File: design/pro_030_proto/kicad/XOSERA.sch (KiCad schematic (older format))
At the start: 38 parts, among them IC16 74LS74, IC17 74HCT245, IC18 74HCT245, IC19 74HCT245, J10 Upduino_LHS, J11 Upduino_RHS, J12 Conn_01x06_Male, J13 PMOD_TOP, J14 PMOD_BOTTOM, J15 Conn_02x04_Counter_Clockwise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

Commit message: More tidy up
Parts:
- R34, R35, R36, R37, R38, R39, R40, R41: value R -> 100R
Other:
- note added: "All 100R"
- note removed: "All 470R"
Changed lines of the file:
@@
 P 5950 4600
 F 0 "R34" V 5950 4600 50  0000 C CNN
-F 1 "R" V 5834 4600 50  0001 C CNN
+F 1 "100R" V 5834 4600 50  0001 C CNN
 F 2 "rosco_m68k:R-0207_10" V 5880 4600 50  0001 C CNN
 F 3 "~" H 5950 4600 50  0001 C CNN
@@
 P 5950 4700
 F 0 "R35" V 5950 4700 50  0000 C CNN
-F 1 "R" V 5834 4700 50  0001 C CNN
+F 1 "100R" V 5834 4700 50  0001 C CNN
 F 2 "rosco_m68k:R-0207_10" V 5880 4700 50  0001 C CNN
 F 3 "~" H 5950 4700 50  0001 C CNN
@@
 P 5950 4800
 F 0 "R36" V 5950 4800 50  0000 C CNN
-F 1 "R" V 5834 4800 50  0001 C CNN
+F 1 "100R" V 5834 4800 50  0001 C CNN
 F 2 "rosco_m68k:R-0207_10" V 5880 4800 50  0001 C CNN
 F 3 "~" H 5950 4800 50  0001 C CNN
@@
 P 5950 4900
 F 0 "R37" V 5950 4900 50  0000 C CNN
-F 1 "R" V 5834 4900 50  0001 C CNN
+F 1 "100R" V 5834 4900 50  0001 C CNN
 F 2 "rosco_m68k:R-0207_10" V 5880 4900 50  0001 C CNN
 F 3 "~" H 5950 4900 50  0001 C CNN
@@
 P 5950 5000
 F 0 "R38" V 5950 5000 50  0000 C CNN
-F 1 "R" V 5834 5000 50  0001 C CNN
+F 1 "100R" V 5834 5000 50  0001 C CNN
 F 2 "rosco_m68k:R-0207_10" V 5880 5000 50  0001 C CNN
 F 3 "~" H 5950 5000 50  0001 C CNN
@@
 P 5950 5100
 F 0 "R39" V 5950 5100 50  0000 C CNN
-F 1 "R" V 5834 5100 50  0001 C CNN
+F 1 "100R" V 5834 5100 50  0001 C CNN
 F 2 "rosco_m68k:R-0207_10" V 5880 5100 50  0001 C CNN
 F 3 "~" H 5950 5100 50  0001 C CNN
@@
 P 5950 5300
 F 0 "R41" V 5950 5300 50  0000 C CNN
-F 1 "R" V 5834 5300 50  0001 C CNN
+F 1 "100R" V 5834 5300 50  0001 C CNN
 F 2 "rosco_m68k:R-0207_10" V 5880 5300 50  0001 C CNN
 F 3 "~" H 5950 5300 50  0001 C CNN
@@
 P 5950 5200
 F 0 "R40" V 5950 5200 50  0000 C CNN
-F 1 "R" V 5834 5200 50  0001 C CNN
+F 1 "100R" V 5834 5200 50  0001 C CNN
 F 2 "rosco_m68k:R-0207_10" V 5880 5200 50  0001 C CNN
 F 3 "~" H 5950 5200 50  0001 C CNN
@@
 $EndComp
 Text Notes 5800 5450 0    50   ~ 0
-All 470R
+All 100R
 Wire Wire Line
 	5800 4600 5700 4600

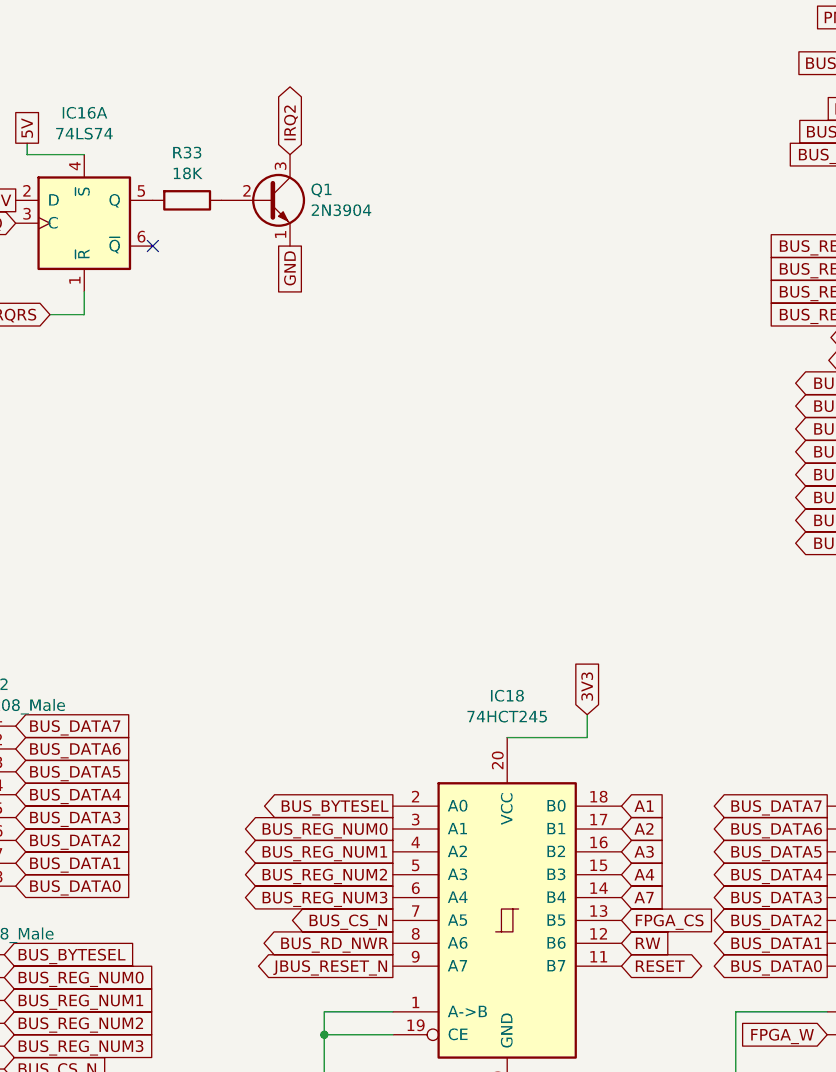
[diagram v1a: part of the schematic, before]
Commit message: Fix incorrect address line hookup for Xosera
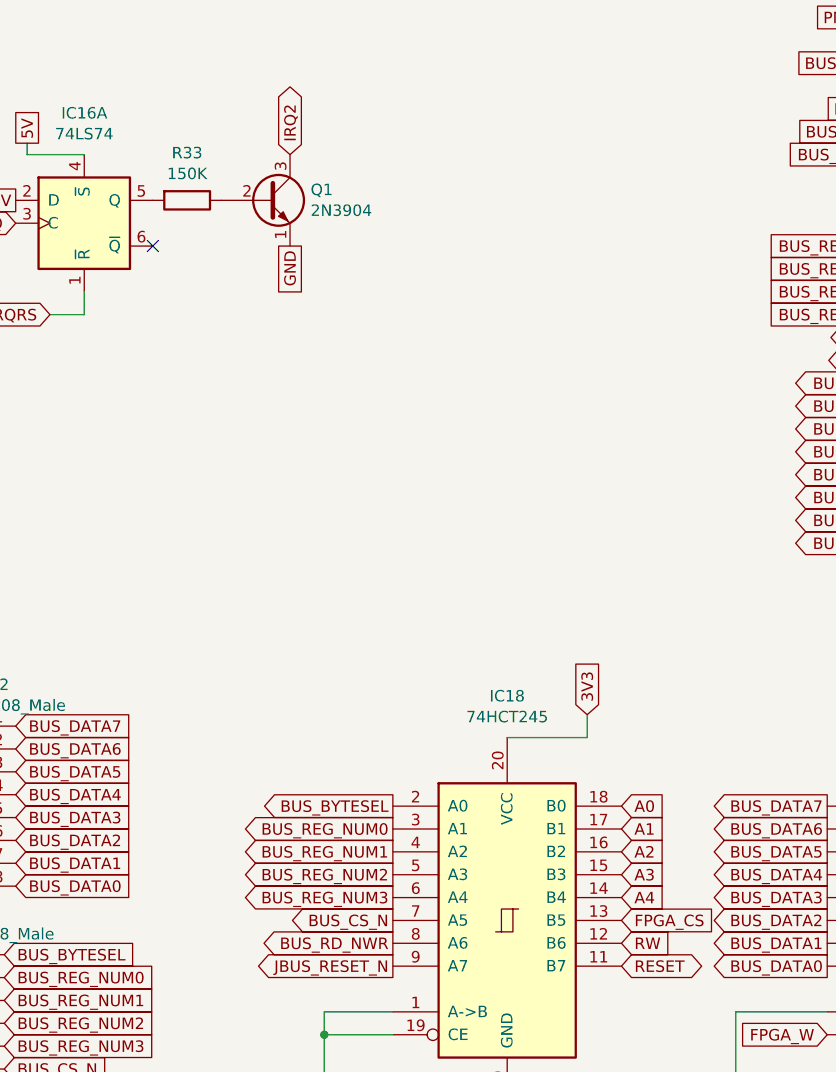
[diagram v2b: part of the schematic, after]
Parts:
- R33: value 18K -> 150K
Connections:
- net A7 is gone; now on net A4: IC18.14 (B4)
- net A1: now also IC18.17 (B1); no longer IC18.18 (B0)
- net A2: now also IC18.16 (B2); no longer IC18.17 (B1)
- net A3: now also IC18.15 (B3); no longer IC18.16 (B2)
- net A4: no longer IC18.15 (B3)
- new net A0: IC18.18 (B0)
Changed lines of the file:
@@
 FPGA_R
 Text GLabel 3800 4600 2    50   Input ~ 0
+A0
+Text GLabel 3800 4700 2    50   Input ~ 0
 A1
-Text GLabel 3800 4700 2    50   Input ~ 0
+Text GLabel 3800 4800 2    50   Input ~ 0
 A2
-Text GLabel 3800 4800 2    50   Input ~ 0
+Text GLabel 3800 4900 2    50   Input ~ 0
 A3
-Text GLabel 3800 4900 2    50   Input ~ 0
+Text GLabel 3800 5000 2    50   Input ~ 0
 A4
-Text GLabel 3800 5000 2    50   Input ~ 0
-A7
 Text GLabel 2800 4600 0    50   Output ~ 0
 BUS_BYTESEL
@@
 P 1900 1950
 F 0 "R33" V 1693 1950 50  0000 C CNN
-F 1 "18K" V 1784 1950 50  0000 C CNN
+F 1 "150K" V 1784 1950 50  0000 C CNN
 F 2 "rosco_m68k:R-0207_10" V 1830 1950 50  0001 C CNN
 F 3 "~" H 1900 1950 50  0001 C CNN

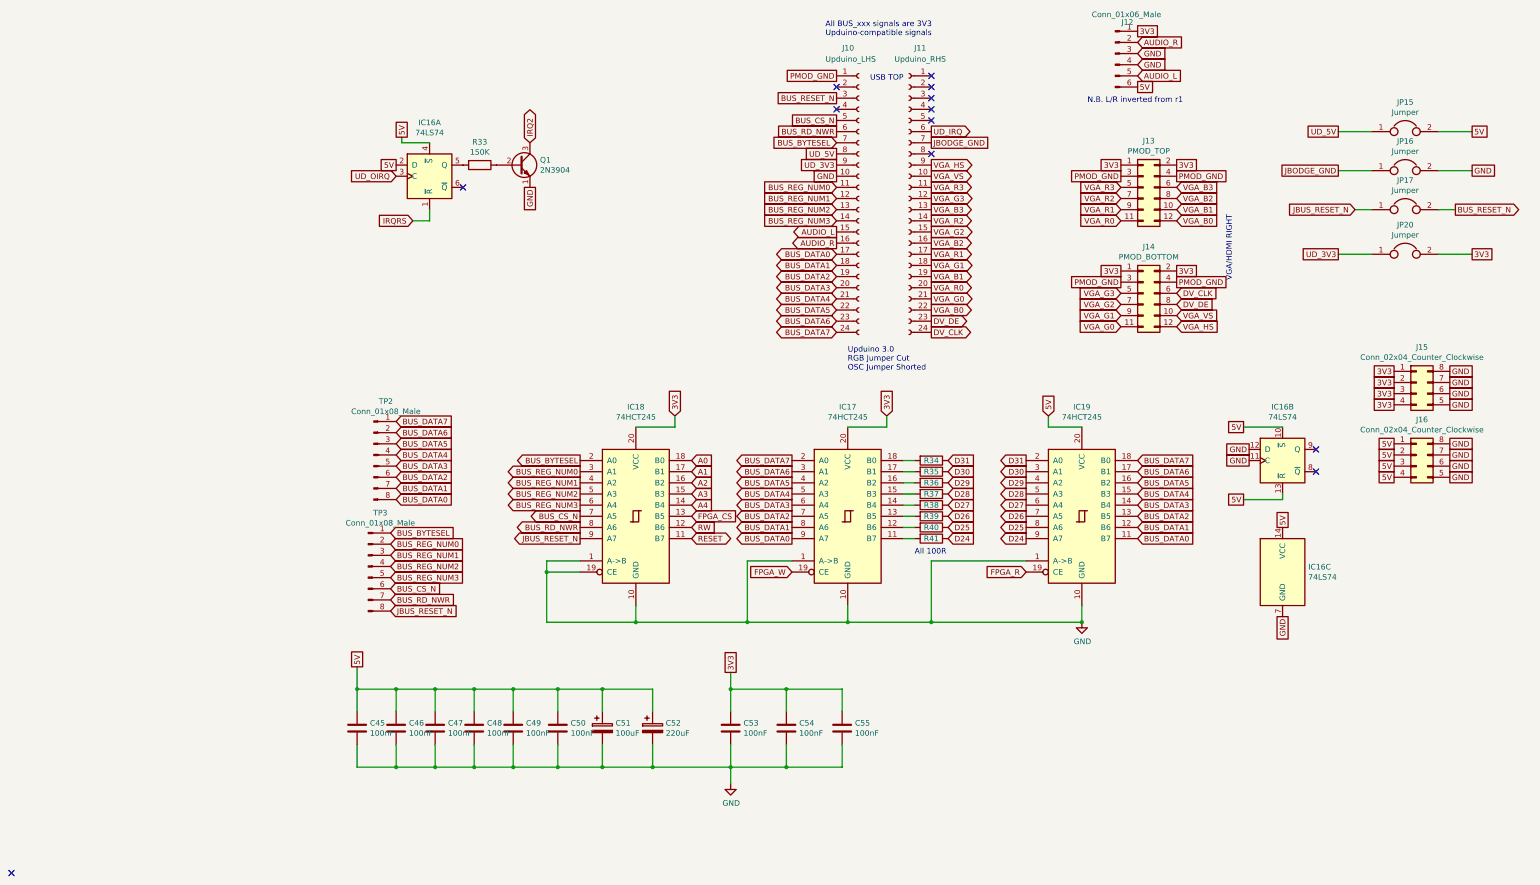
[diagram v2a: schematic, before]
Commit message: Add new Xosera DTACK stretch GAL
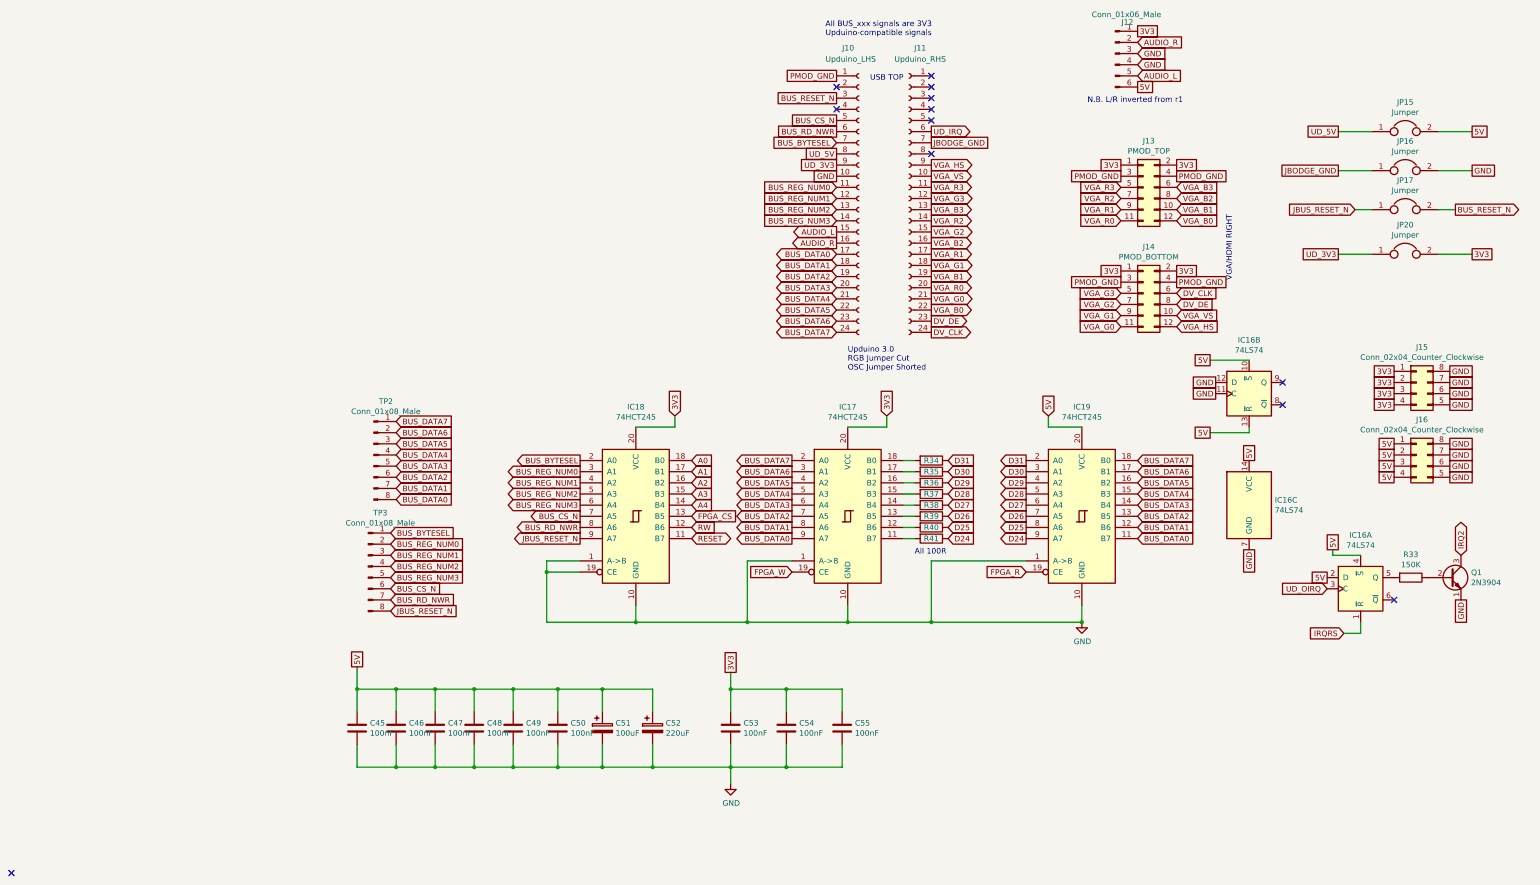
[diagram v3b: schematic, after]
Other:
- moved on the sheet: IC16A, IC16B, IC16C, Q1, R33
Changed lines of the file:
@@
 L 74xx:74LS74 IC16
 U 1 1 60D12D20
-P 1450 2050
-F 0 "IC16" H 1450 2531 50  0000 C CNN
-F 1 "74LS74" H 1450 2440 50  0000 C CNN
-F 2 "Package_DIP:DIP-14_W7.62mm_Socket_LongPads" H 1450 2050 50  0001 C CNN
-F 3 "74xx/74hc_hct74.pdf" H 1450 2050 50  0001 C CNN
-	1    1450 2050
+P 9800 5750
+F 0 "IC16" H 9800 6231 50  0000 C CNN
+F 1 "74LS74" H 9800 6140 50  0000 C CNN
+F 2 "Package_DIP:DIP-14_W7.62mm_Socket_LongPads" H 9800 5750 50  0001 C CNN
+F 3 "74xx/74hc_hct74.pdf" H 9800 5750 50  0001 C CNN
+	1    9800 5750
 	1    0    0    -1
 $EndComp
@@
 L Transistor_BJT:2N3904 Q1
 U 1 1 60D18FD6
-P 2250 1950
-F 0 "Q1" H 2440 1996 50  0000 L CNN
-F 1 "2N3904" H 2440 1905 50  0000 L CNN
-F 2 "Package_TO_SOT_THT:TO-92_HandSolder" H 2450 1875 50  0001 L CIN
-F 3 "https://www.fairchildsemi.com/datasheets/2N/2N3904.pdf" H 2250 1950 50  0001 L CNN
-	1    2250 1950
+P 10600 5650
+F 0 "Q1" H 10790 5696 50  0000 L CNN
+F 1 "2N3904" H 10790 5605 50  0000 L CNN
+F 2 "Package_TO_SOT_THT:TO-92_HandSolder" H 10800 5575 50  0001 L CIN
+F 3 "https://www.fairchildsemi.com/datasheets/2N/2N3904.pdf" H 10600 5650 50  0001 L CNN
+	1    10600 5650
 	1    0    0    -1
 $EndComp
@@
 L Device:R R33
 U 1 1 60D232A8
-P 1900 1950
-F 0 "R33" V 1693 1950 50  0000 C CNN
-F 1 "150K" V 1784 1950 50  0000 C CNN
-F 2 "rosco_m68k:R-0207_10" V 1830 1950 50  0001 C CNN
-F 3 "~" H 1900 1950 50  0001 C CNN
-	1    1900 1950
+P 10250 5650
+F 0 "R33" V 10043 5650 50  0000 C CNN
+F 1 "150K" V 10134 5650 50  0000 C CNN
+F 2 "rosco_m68k:R-0207_10" V 10180 5650 50  0001 C CNN
+F 3 "~" H 10250 5650 50  0001 C CNN
+	1    10250 5650
 	0    1    1    0
 $EndComp
-Text GLabel 1150 1950 0    50   UnSpc ~ 0
+Text GLabel 9500 5650 0    50   UnSpc ~ 0
 5V
-Text GLabel 1150 2050 0    50   Input ~ 0
+Text GLabel 9500 5750 0    50   Input ~ 0
 UD_OIRQ
-NoConn ~ 1750 2150
-Text GLabel 1300 2450 0    50   Input ~ 0
+NoConn ~ 10100 5850
+Text GLabel 9650 6150 0    50   Input ~ 0
 IRQRS
 Wire Wire Line
-	1300 2450 1450 2450
+	9650 6150 9800 6150
 Wire Wire Line
-	1450 2450 1450 2350
-Text GLabel 1200 1700 1    50   UnSpc ~ 0
+	9800 6150 9800 6050
+Text GLabel 9550 5400 1    50   UnSpc ~ 0
 5V
 Wire Wire Line
-	1200 1700 1200 1750
+	9550 5400 9550 5450
 Wire Wire Line
-	1200 1750 1450 1750
-Text GLabel 2350 2150 3    50   UnSpc ~ 0
+	9550 5450 9800 5450
+Text GLabel 10700 5850 3    50   UnSpc ~ 0
 GND
-Text GLabel 2350 1750 1    50   3State ~ 0
+Text GLabel 10700 5450 1    50   3State ~ 0
 IRQ2
 $Comp
 L 74xx:74LS74 IC16
 U 3 1 60D60650
-P 9100 5600
-F 0 "IC16" H 9330 5646 50  0000 L CNN
-F 1 "74LS74" H 9330 5555 50  0000 L CNN
-F 2 "Package_DIP:DIP-14_W7.62mm_Socket_LongPads" H 9100 5600 50  0001 C CNN
-F 3 "74xx/74hc_hct74.pdf" H 9100 5600 50  0001 C CNN
-	3    9100 5600
+P 8800 5000
+F 0 "IC16" H 9030 5046 50  0000 L CNN
+F 1 "74LS74" H 9030 4955 50  0000 L CNN
+F 2 "Package_DIP:DIP-14_W7.62mm_Socket_LongPads" H 8800 5000 50  0001 C CNN
+F 3 "74xx/74hc_hct74.pdf" H 8800 5000 50  0001 C CNN
+	3    8800 5000
 	1    0    0    -1
 $EndComp
-Text GLabel 9100 5200 1    50   UnSpc ~ 0
+Text GLabel 8800 4600 1    50   UnSpc ~ 0
 5V
-Text GLabel 9100 6000 3    50   UnSpc ~ 0
+Text GLabel 8800 5400 3    50   UnSpc ~ 0
 GND
 $Comp
 L 74xx:74LS74 IC16
 U 2 1 60D7C1C9
-P 9100 4600
-F 0 "IC16" H 9100 5081 50  0000 C CNN
-F 1 "74LS74" H 9100 4990 50  0000 C CNN
-F 2 "Package_DIP:DIP-14_W7.62mm_Socket_LongPads" H 9100 4600 50  0001 C CNN
-F 3 "74xx/74hc_hct74.pdf" H 9100 4600 50  0001 C CNN
-	2    9100 4600
+P 8800 4000
+F 0 "IC16" H 8800 4481 50  0000 C CNN
+F 1 "74LS74" H 8800 4390 50  0000 C CNN
+F 2 "Package_DIP:DIP-14_W7.62mm_Socket_LongPads" H 8800 4000 50  0001 C CNN
+F 3 "74xx/74hc_hct74.pdf" H 8800 4000 50  0001 C CNN
+	2    8800 4000
 	1    0    0    -1
 $EndComp
-Text GLabel 8800 4500 0    50   UnSpc ~ 0
+Text GLabel 8500 3900 0    50   UnSpc ~ 0
 GND
-Text GLabel 8800 4600 0    50   UnSpc ~ 0
+Text GLabel 8500 4000 0    50   UnSpc ~ 0
 GND
-Text GLabel 8750 4300 0    50   UnSpc ~ 0
+Text GLabel 8450 3700 0    50   UnSpc ~ 0
 5V
-Text GLabel 8750 4950 0    50   UnSpc ~ 0
+Text GLabel 8450 4350 0    50   UnSpc ~ 0
 5V
 Wire Wire Line
-	8750 4950 9100 4950
+	8450 4350 8800 4350
 Wire Wire Line
-	9100 4950 9100 4900
-NoConn ~ 9400 4500
-NoConn ~ 9400 4700
+	8800 4350 8800 4300
+NoConn ~ 9100 3900
+NoConn ~ 9100 4100
 $Comp
 L Device:Jumper JP17
@@
 Connection ~ 7300 6050
 Wire Wire Line
-	8750 4300 9100 4300
+	8450 3700 8800 3700
 Wire Wire Line
 	3300 6050 4300 6050
